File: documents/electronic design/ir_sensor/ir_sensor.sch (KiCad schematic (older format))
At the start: 11 parts, among them J2 Conn_01x01, U2 STM32F103HEADER, U3 MPU6050_module, U4 SE8R01_module

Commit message: adjust pcb
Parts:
- J1, J3, J4, J5, J6, J7: renamed from J?; footprint (none) -> Pin_Headers:Pin_Header_Straight_1x06_Pitch2.54mm
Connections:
- net SE8R01_IRQ: now also U2.1 (B12); no longer U2.7 (A10)
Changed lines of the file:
@@
 Text GLabel 4300 1200 0    60   Input ~ 0
 SE8R01_CSN
-Text GLabel 4300 1400 0    60   Input ~ 0
+Text GLabel 4300 800  0    60   Input ~ 0
 SE8R01_IRQ
 Text GLabel 2200 2600 2    60   Input ~ 0
@@
 	-1   0    0    1
 $EndComp
-NoConn ~ 4300 800
 Text GLabel 4300 1300 0    60   Input ~ 0
 SE8R01_CE
@@
 $EndComp
 $Comp
-L Conn_01x06 J?
+L Conn_01x06 J3
 U 1 1 59FC2749
 P 1500 4200
-F 0 "J?" H 1500 4500 50  0000 C CNN
+F 0 "J3" H 1500 4500 50  0000 C CNN
 F 1 "Conn_01x06" H 1500 3800 50  0000 C CNN
-F 2 "" H 1500 4200 50  0001 C CNN
+F 2 "Pin_Headers:Pin_Header_Straight_1x06_Pitch2.54mm" H 1500 4200 50  0001 C CNN
 F 3 "" H 1500 4200 50  0001 C CNN
 	1    1500 4200
@@
 $EndComp
 $Comp
-L Conn_01x06 J?
+L Conn_01x06 J5
 U 1 1 59FC2827
 P 2300 4200
-F 0 "J?" H 2300 4500 50  0000 C CNN
+F 0 "J5" H 2300 4500 50  0000 C CNN
 F 1 "Conn_01x06" H 2300 3800 50  0000 C CNN
-F 2 "" H 2300 4200 50  0001 C CNN
+F 2 "Pin_Headers:Pin_Header_Straight_1x06_Pitch2.54mm" H 2300 4200 50  0001 C CNN
 F 3 "" H 2300 4200 50  0001 C CNN
 	1    2300 4200
@@
 $EndComp
 $Comp
-L Conn_01x06 J?
+L Conn_01x06 J7
 U 1 1 59FC2879
 P 3100 4200
-F 0 "J?" H 3100 4500 50  0000 C CNN
+F 0 "J7" H 3100 4500 50  0000 C CNN
 F 1 "Conn_01x06" H 3100 3800 50  0000 C CNN
-F 2 "" H 3100 4200 50  0001 C CNN
+F 2 "Pin_Headers:Pin_Header_Straight_1x06_Pitch2.54mm" H 3100 4200 50  0001 C CNN
 F 3 "" H 3100 4200 50  0001 C CNN
 	1    3100 4200
@@
 $EndComp
 $Comp
-L Conn_01x06 J?
+L Conn_01x06 J1
 U 1 1 59FC2A4E
 P 1500 3400
-F 0 "J?" H 1500 3700 50  0000 C CNN
+F 0 "J1" H 1500 3700 50  0000 C CNN
 F 1 "Conn_01x06" H 1500 3000 50  0000 C CNN
-F 2 "" H 1500 3400 50  0001 C CNN
+F 2 "Pin_Headers:Pin_Header_Straight_1x06_Pitch2.54mm" H 1500 3400 50  0001 C CNN
 F 3 "" H 1500 3400 50  0001 C CNN
 	1    1500 3400
@@
 $EndComp
 $Comp
-L Conn_01x06 J?
+L Conn_01x06 J4
 U 1 1 59FC2A54
 P 2300 3400
-F 0 "J?" H 2300 3700 50  0000 C CNN
+F 0 "J4" H 2300 3700 50  0000 C CNN
 F 1 "Conn_01x06" H 2300 3000 50  0000 C CNN
-F 2 "" H 2300 3400 50  0001 C CNN
+F 2 "Pin_Headers:Pin_Header_Straight_1x06_Pitch2.54mm" H 2300 3400 50  0001 C CNN
 F 3 "" H 2300 3400 50  0001 C CNN
 	1    2300 3400
@@
 $EndComp
 $Comp
-L Conn_01x06 J?
+L Conn_01x06 J6
 U 1 1 59FC2A5A
 P 3100 3400
-F 0 "J?" H 3100 3700 50  0000 C CNN
+F 0 "J6" H 3100 3700 50  0000 C CNN
 F 1 "Conn_01x06" H 3100 3000 50  0000 C CNN
-F 2 "" H 3100 3400 50  0001 C CNN
+F 2 "Pin_Headers:Pin_Header_Straight_1x06_Pitch2.54mm" H 3100 3400 50  0001 C CNN
 F 3 "" H 3100 3400 50  0001 C CNN
 	1    3100 3400
@@
 Connection ~ 1900 3300
 $Comp
-L GND #PWR?
+L GND #PWR012
 U 1 1 59FC2E26
 P 1900 4250
-F 0 "#PWR?" H 1900 4000 50  0001 C CNN
+F 0 "#PWR012" H 1900 4000 50  0001 C CNN
 F 1 "GND" H 1900 4100 50  0000 C CNN
 F 2 "" H 1900 4250 50  0000 C CNN
@@
 Connection ~ 2700 4100
 $Comp
-L +3V3 #PWR?
+L +3V3 #PWR013
 U 1 1 59FC2F1A
 P 2700 3450
-F 0 "#PWR?" H 2700 3300 50  0001 C CNN
+F 0 "#PWR013" H 2700 3300 50  0001 C CNN
 F 1 "+3V3" H 2700 3590 50  0000 C CNN
 F 2 "" H 2700 3450 50  0000 C CNN
@@
 $EndComp
 $Comp
-L +3V3 #PWR?
+L +3V3 #PWR014
 U 1 1 59FC2FFF
 P 2700 4250
-F 0 "#PWR?" H 2700 4100 50  0001 C CNN
+F 0 "#PWR014" H 2700 4100 50  0001 C CNN
 F 1 "+3V3" H 2700 4390 50  0000 C CNN
 F 2 "" H 2700 4250 50  0000 C CNN
@@
 	0    -1   -1   0
 $EndComp
+NoConn ~ 4300 1400
 $EndSCHEMATC

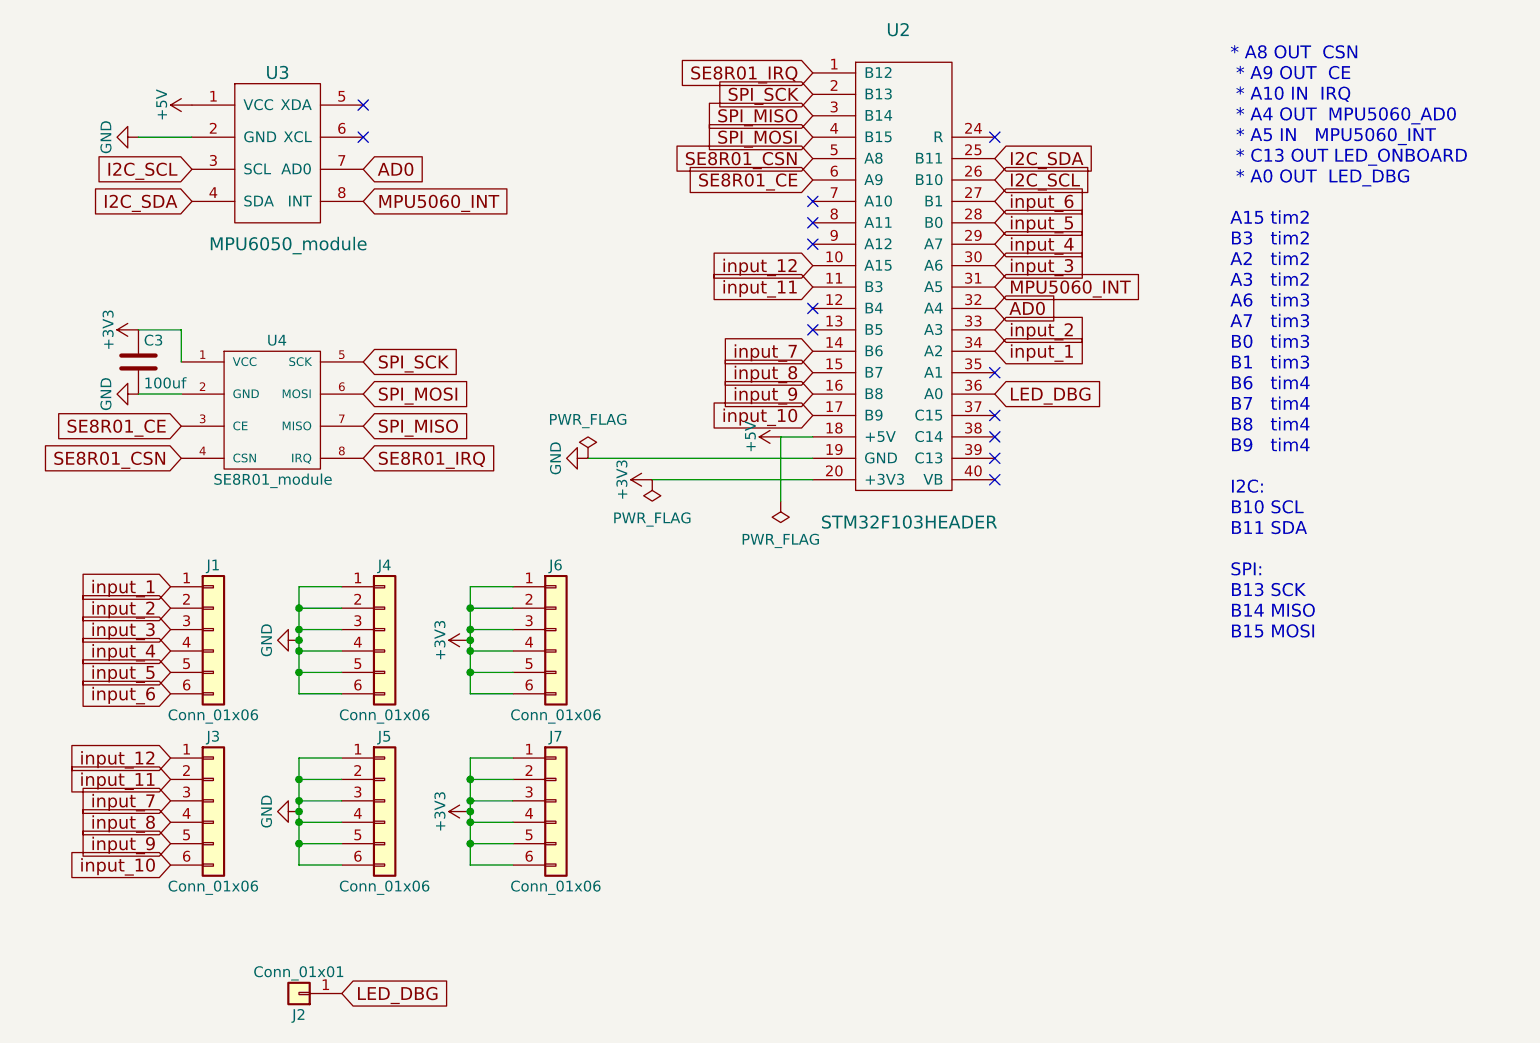
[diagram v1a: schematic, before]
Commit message: adjust pcb, pin assignments
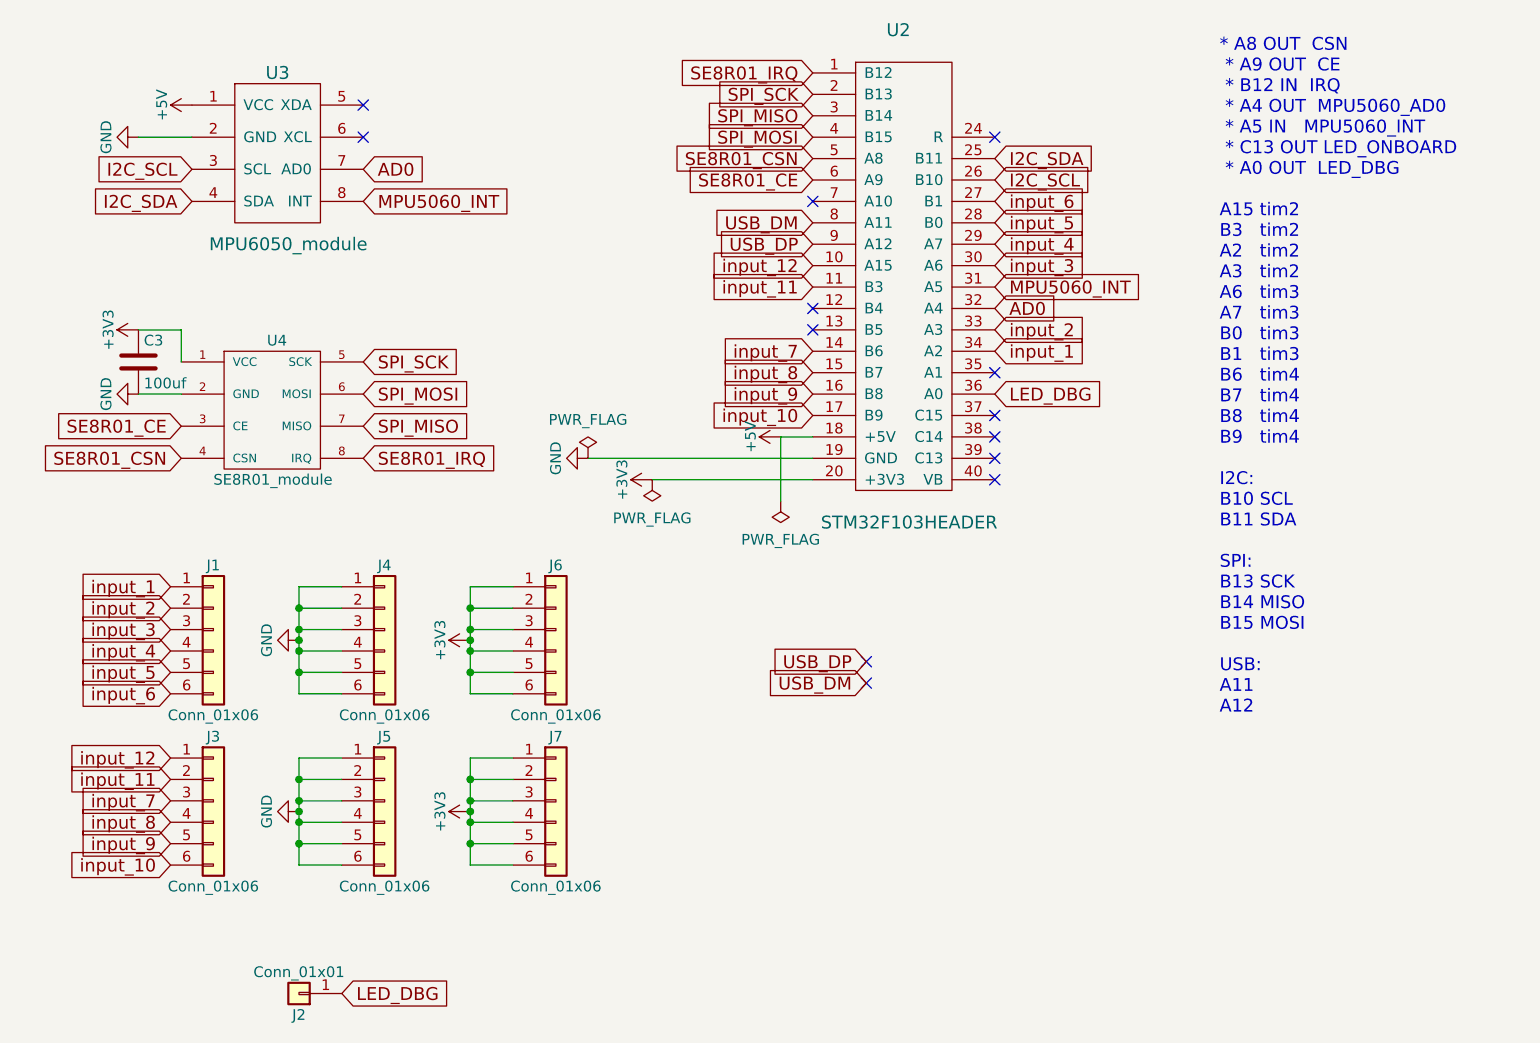
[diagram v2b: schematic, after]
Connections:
- net USB_DM: now reaches U2.8 (A11)
- net USB_DP: now reaches U2.9 (A12)
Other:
- note added: "* A8 OUT CSN \n * A9 OUT CE \n * B12 IN IRQ \n * A4 OUT MPU5060_AD0 \n * A5 IN MPU5060_INT \n * C13 OUT LED_ONBOARD \n * A0 OUT LED_DBG \n\nA15 tim2\nB3 tim2\nA2 tim2\nA3 tim2\nA6 tim3\nA7 tim3\nB0 tim3\nB1 tim3\nB6 tim4\nB7 tim4\nB8 tim4\nB9 tim4\n\nI2C:\nB10 SCL\nB11 SDA\n\nSPI:\nB13 SCK\nB14 MISO\nB15 MOSI\n\nUSB:\nA11\nA12\n"
- note removed: "* A8 OUT CSN \n * A9 OUT CE \n * A10 IN IRQ \n * A4 OUT MPU5060_AD0 \n * A5 IN MPU5060_INT \n * C13 OUT LED_ONBOARD \n * A0 OUT LED_DBG \n\nA15 tim2\nB3 tim2\nA2 tim2\nA3 tim2\nA6 tim3\nA7 tim3\nB0 tim3\nB1 tim3\nB6 tim4\nB7 tim4\nB8 tim4\nB9 tim4\n\nI2C:\nB10 SCL\nB11 SDA\n\nSPI:\nB13 SCK\nB14 MISO\nB15 MOSI\n\n"
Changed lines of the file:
@@
 Text GLabel 1400 1250 0    60   Input ~ 0
 I2C_SCL
-Text Notes 6250 3550 0    60   ~ 0
- * A8 OUT  CSN \n * A9 OUT  CE  \n * A10 IN  IRQ \n * A4 OUT  MPU5060_AD0 \n * A5 IN   MPU5060_INT \n * C13 OUT LED_ONBOARD \n * A0 OUT  LED_DBG  \n\nA15 tim2\nB3   tim2\nA2   tim2\nA3   tim2\nA6   tim3\nA7   tim3\nB0   tim3\nB1   tim3\nB6   tim4\nB7   tim4\nB8   tim4\nB9   tim4\n\nI2C:\nB10 SCL\nB11 SDA\n\nSPI:\nB13 SCK\nB14 MISO\nB15 MOSI\n\n
+Text Notes 6200 3800 0    60   ~ 0
+ * A8 OUT  CSN \n * A9 OUT  CE  \n * B12 IN  IRQ \n * A4 OUT  MPU5060_AD0 \n * A5 IN   MPU5060_INT \n * C13 OUT LED_ONBOARD \n * A0 OUT  LED_DBG  \n\nA15 tim2\nB3   tim2\nA2   tim2\nA3   tim2\nA6   tim3\nA7   tim3\nB0   tim3\nB1   tim3\nB6   tim4\nB7   tim4\nB8   tim4\nB9   tim4\n\nI2C:\nB10 SCL\nB11 SDA\n\nSPI:\nB13 SCK\nB14 MISO\nB15 MOSI\n\nUSB:\nA11\nA12\n
 Text GLabel 5150 1900 2    60   Input ~ 0
 AD0
@@
 Text GLabel 2200 2450 2    60   Input ~ 0
 SPI_MISO
-NoConn ~ 4300 1600
 NoConn ~ 4300 1900
 NoConn ~ 4300 2000
@@
 LED_DBG
 NoConn ~ 5150 2200
-NoConn ~ 4300 1500
 Text GLabel 1300 3200 0    60   Input ~ 0
 input_1
@@
 $EndComp
 NoConn ~ 4300 1400
+Text GLabel 4550 3550 0    60   Input ~ 0
+USB_DP
+Text GLabel 4550 3650 0    60   Input ~ 0
+USB_DM
+NoConn ~ 4550 3550
+NoConn ~ 4550 3650
+Text GLabel 4300 1500 0    60   Input ~ 0
+USB_DM
+Text GLabel 4300 1600 0    60   Input ~ 0
+USB_DP
 $EndSCHEMATC
